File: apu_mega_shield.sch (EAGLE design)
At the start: 36 parts, among them IC1 74HCT573D, IC2 4050D, IC3 DS1307, Q1 32.768, U1 IS62C1024AL-35QLI, X1 MICROSD

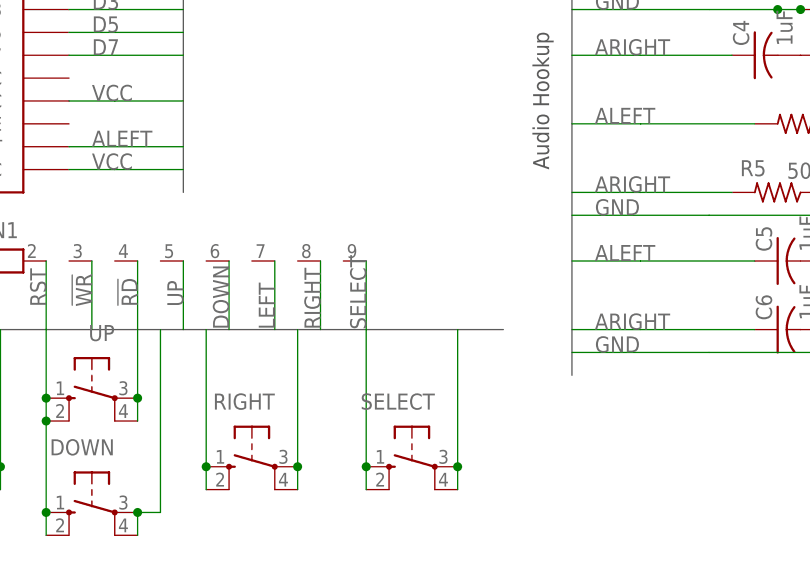
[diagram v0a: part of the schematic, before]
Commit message: Micro SD card detect pullup resistor added.
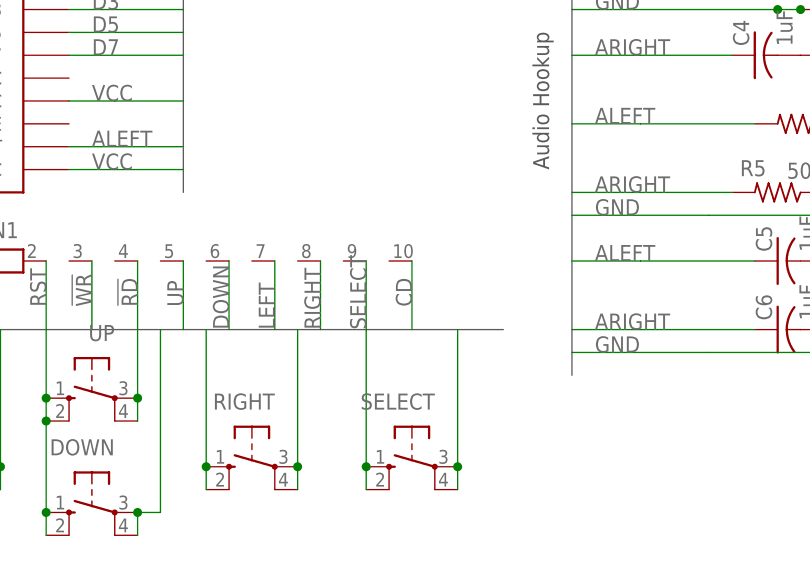
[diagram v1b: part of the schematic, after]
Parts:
- C1, C2, C7: device resistor:C-EUC0603 -> rcl:C-EUC0805
- RN1: device resistor-net:RN08 -> resistor-net:RN09
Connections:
- net CD: now also RN1.10
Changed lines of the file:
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@@
 <part name="APU" library="switch-omron" deviceset="10-XX" device="" value="Reset"/>
 <part name="U$6" library="E14_Arduino_revB" deviceset="ARDUINO_MEGA_2560_LITE" device="NO_LABELS" value="ARDUINO_MEGA_2560_LITENO_LABELS"/>
-<part name="C1" library="resistor" deviceset="C-EU" device="C0603" value="100nF"/>
-<part name="C2" library="resistor" deviceset="C-EU" device="C0603" value="100nF"/>
-<part name="C7" library="resistor" deviceset="C-EU" device="C0603" value="100nF"/>
+<part name="C1" library="rcl" deviceset="C-EU" device="C0805" value="100nF"/>
+<part name="C2" library="rcl" deviceset="C-EU" device="C0805" value="100nF"/>
+<part name="C7" library="rcl" deviceset="C-EU" device="C0805" value="100nF"/>
 <part name="IC1" library="74xx-eu" deviceset="74*573" device="D" technology="HCT"/>
 <part name="U1" library="ISSI_By_element14_Batch_1" deviceset="IS62C1024AL-35QLI" device=""/>
@@
 <part name="RIGHT" library="switch-omron" deviceset="10-XX" device=""/>
 <part name="SELECT" library="switch-omron" deviceset="10-XX" device=""/>
-<part name="RN1" library="resistor-net" deviceset="RN08" device=""/>
+<part name="RN1" library="resistor-net" deviceset="RN09" device=""/>
 <part name="Q1" library="crystal" deviceset="CRYTAL" device="TC38H" value="32.768"/>
 <part name="IC3" library="adafruit" deviceset="DS1307" device=""/>
@@
 <bus name="RST,!WR,!RD,UP,DOWN,LEFT,RIGHT,SELECT,VCC,GND">
 <segment>
+<wire x1="246.38" y1="78.74" x2="223.52" y2="78.74" width="0.762" layer="92"/>
+</segment>
+</bus>
+<bus name="RST,!WR,!RD,UP,DOWN,LEFT,RIGHT,SELECT,VCC,GND,CD">
+<segment>
 <wire x1="193.04" y1="10.16" x2="106.68" y2="10.16" width="0.762" layer="92"/>
-</segment>
-<segment>
-<wire x1="246.38" y1="78.74" x2="223.52" y2="78.74" width="0.762" layer="92"/>
 </segment>
 </bus>
@@
 <label x="262.89" y="99.06" size="1.778" layer="95"/>
 </segment>
-</net>
+<segment>
+<pinref part="RN1" gate="1" pin="10"/>
+<wire x1="182.88" y1="17.78" x2="182.88" y2="10.16" width="0.1524" layer="91"/>
+<label x="182.88" y="12.7" size="1.778" layer="95" rot="R90"/>
+</segment>
+</net>
